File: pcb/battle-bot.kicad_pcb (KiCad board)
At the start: 4 copper layers, 0 parts

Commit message: Place power connectors
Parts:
- added REF**: AMASS_XT30PW-M_1x02_P2.50mm_Horizontal, Connector_AMASS:AMASS_XT30PW-M_1x02_P2.50mm_Horizontal, F.Cu at (73.2, 53.8)
- added REF**: AMASS_XT30PW-M_1x02_P2.50mm_Horizontal, Connector_AMASS:AMASS_XT30PW-M_1x02_P2.50mm_Horizontal, F.Cu at (132.7, 56.6)
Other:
- board outline added: 99.2 x 51.2 mm

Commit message: Save
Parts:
- added C1: 22u, Capacitor_SMD:C_1206_3216Metric, F.Cu at (154.3, 87.5)
- added C2: 22u, Capacitor_SMD:C_1206_3216Metric, F.Cu at (154.3, 90.8)
- added C3: 10n, Capacitor_SMD:C_0402_1005Metric, F.Cu at (165.1, 69.9)
- added C4: 47u, Capacitor_SMD:C_1206_3216Metric, F.Cu at (154.3, 94.2)
- added C5: 47u, Capacitor_SMD:C_1206_3216Metric, F.Cu at (154.3, 97.5)
- added C6: 47u, Capacitor_SMD:C_1206_3216Metric, F.Cu at (154.3, 100.9)
- added D3: B5819W, Diode_SMD:D_SOD-123, F.Cu at (160.1, 101.8)
- added L1: 15u, Inductor_SMD:L_Changjiang_FNR6020S, F.Cu at (161.0, 96.3)
- added R1: R, Resistor_SMD:R_0402_1005Metric, F.Cu at (164.4, 101.1)
- added R2: R, Resistor_SMD:R_0402_1005Metric, F.Cu at (164.4, 103.1)
- added REF**: BGA-16_1.92x1.92mm_Layout4x4_P0.5mm, Package_BGA:BGA-16_1.92x1.92mm_Layout4x4_P0.5mm, F.Cu at (92.0, 67.3)
- added REF**: BGA-16_1.92x1.92mm_Layout4x4_P0.5mm, Package_BGA:BGA-16_1.92x1.92mm_Layout4x4_P0.5mm, F.Cu at (108.0, 71.8)
- added REF**: BGA-16_1.92x1.92mm_Layout4x4_P0.5mm, Package_BGA:BGA-16_1.92x1.92mm_Layout4x4_P0.5mm, F.Cu at (86.8, 71.8)
- added REF**: BGA-16_1.92x1.92mm_Layout4x4_P0.5mm, Package_BGA:BGA-16_1.92x1.92mm_Layout4x4_P0.5mm, F.Cu at (102.7, 67.3)
- added REF**: BGA-16_1.92x1.92mm_Layout4x4_P0.5mm, Package_BGA:BGA-16_1.92x1.92mm_Layout4x4_P0.5mm, F.Cu at (113.3, 71.8)
- added REF**: TFBGA-100_8x8mm_Layout10x10_P0.8mm, Package_BGA:TFBGA-100_8x8mm_Layout10x10_P0.8mm, F.Cu at (160.4, 79.2)
- added REF**: PowerPAK_SO-8_Single, Package_SO:PowerPAK_SO-8_Single, F.Cu at (126.4, 61.9)
- added REF**: R_0402_1005Metric, Resistor_SMD:R_0402_1005Metric, F.Cu at (92.6, 64.5)
- added REF**: BGA-16_1.92x1.92mm_Layout4x4_P0.5mm, Package_BGA:BGA-16_1.92x1.92mm_Layout4x4_P0.5mm, F.Cu at (113.3, 67.2)
- added REF**: PowerPAK_SO-8_Single, Package_SO:PowerPAK_SO-8_Single, F.Cu at (74.4, 61.7)
- added REF**: BGA-16_1.92x1.92mm_Layout4x4_P0.5mm, Package_BGA:BGA-16_1.92x1.92mm_Layout4x4_P0.5mm, F.Cu at (97.3, 71.8)
- added REF**: BGA-16_1.92x1.92mm_Layout4x4_P0.5mm, Package_BGA:BGA-16_1.92x1.92mm_Layout4x4_P0.5mm, F.Cu at (92.0, 71.8)
- added REF**: BGA-16_1.92x1.92mm_Layout4x4_P0.5mm, Package_BGA:BGA-16_1.92x1.92mm_Layout4x4_P0.5mm, F.Cu at (102.7, 71.8)
- added U1: TPS5430DDA, Package_SO:TI_SO-PowerPAD-8_ThermalVias, F.Cu at (161.4, 89.2)
- added U2: STM32G474VETx, Package_QFP:LQFP-100_14x14mm_P0.5mm, F.Cu at (100.0, 49.4)
- moved REF** 5.72 mm to (127.6, 54.0)
- moved REF** 4.08 mm to (76.7, 51.7)

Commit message: Finish drivers
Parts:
- removed REF** (x9): BGA-16_1.92x1.92mm_Layout4x4_P0.5mm, Package_BGA:BGA-16_1.92x1.92mm_Layout4x4_P0.5mm
- removed REF** (x2): AMASS_XT30PW-M_1x02_P2.50mm_Horizontal, Connector_AMASS:AMASS_XT30PW-M_1x02_P2.50mm_Horizontal
- removed REF**: TFBGA-100_8x8mm_Layout10x10_P0.8mm, Package_BGA:TFBGA-100_8x8mm_Layout10x10_P0.8mm
- removed REF** (x2): PowerPAK_SO-8_Single, Package_SO:PowerPAK_SO-8_Single
- removed REF**: R_0402_1005Metric, Resistor_SMD:R_0402_1005Metric
- added AE1: Antenna, RF_Antenna:Johanson_2450AT18x100, F.Cu at (120.8, 7.26)
- added C10: 100n, Resistor_SMD:R_0402_1005Metric, F.Cu at (134.7, 13.1)
- added C11: 47u, Capacitor_SMD:C_1206_3216Metric, F.Cu at (117.6, 37.7)
- added C12: 10n, Capacitor_SMD:C_0402_1005Metric, F.Cu at (130.3, 5.78)
- added C13: 33n, Capacitor_SMD:C_0402_1005Metric, F.Cu at (131.7, 7.17)
- added C14: 47u, Capacitor_SMD:C_1206_3216Metric, F.Cu at (117.6, 41.0)
- added C15: 1n, Capacitor_SMD:C_0402_1005Metric, F.Cu at (125.9, 3.86)
- added C16: 47u, Capacitor_SMD:C_1206_3216Metric, F.Cu at (117.6, 44.3)
- added C17: 47u, Capacitor_SMD:C_1206_3216Metric, F.Cu at (117.6, 47.6)
- added C18: 220u, Capacitor_THT:C_Radial_D6.3mm_H7.0mm_P2.50mm, F.Cu at (97.7, 42.8)
- added C19: 2n2, Capacitor_SMD:C_0603_1608Metric, F.Cu at (128.0, 12.1)
- added C20: 12p, Capacitor_SMD:C_0402_1005Metric, F.Cu at (123.6, 12.6)
- added C21: 4p7, Capacitor_SMD:C_0603_1608Metric, F.Cu at (129.8, 13.9)
- added C22: 1p5, Capacitor_SMD:C_0402_1005Metric, F.Cu at (126.4, 15.4)
- added C23: 12p, Capacitor_SMD:C_0402_1005Metric, F.Cu at (122.2, 11.2)
- added C24: 1p, Capacitor_SMD:C_0402_1005Metric, F.Cu at (125.0, 14.0)
- added C25: 10u, Resistor_SMD:R_0402_1005Metric, F.Cu at (136.1, 14.5)
- added C26: 4u7, Capacitor_SMD:C_0402_1005Metric, F.Cu at (119.7, -1.48)
- added C27: 10n, Capacitor_SMD:C_0402_1005Metric, F.Cu at (127.9, 1.83)
- added C28: 220p, Resistor_SMD:R_0402_1005Metric, F.Cu at (137.5, 15.9)
- added C29: 100n, Capacitor_SMD:C_0402_1005Metric, F.Cu at (121.5, 0.22)
- added C30: 100n, Capacitor_SMD:C_0402_1005Metric, F.Cu at (122.9, 1.61)
- added C31: 0p3, Capacitor_SMD:C_0402_1005Metric, F.Cu at (135.8, 3.11)
- added C32: 22u, Resistor_SMD:R_0805_2012Metric, F.Cu at (66.1, 35.9)
- added C33: 1u, Resistor_SMD:R_0402_1005Metric, F.Cu at (65.4, 27.5)
- added C34: 1u, Resistor_SMD:R_0402_1005Metric, F.Cu at (65.4, 29.5)
- added C35: 100n, Capacitor_SMD:C_0402_1005Metric, F.Cu at (74.1, 27.5)
- added C36: 1u, Resistor_SMD:R_0402_1005Metric, F.Cu at (65.4, 31.5)
- added C37: 47n, Capacitor_SMD:C_0402_1005Metric, F.Cu at (74.1, 29.5)
- added C38: 100n, Capacitor_SMD:C_0402_1005Metric, F.Cu at (74.1, 31.4)
- added C39: 22u, Resistor_SMD:R_0805_2012Metric, F.Cu at (106.2, 27.9)
- added C40: 1u, Resistor_SMD:R_0402_1005Metric, F.Cu at (105.5, 19.5)
- added C41: 1u, Resistor_SMD:R_0402_1005Metric, F.Cu at (105.5, 21.5)
- added C42: 100n, Capacitor_SMD:C_0402_1005Metric, F.Cu at (114.2, 19.5)
- added C43: 1u, Resistor_SMD:R_0402_1005Metric, F.Cu at (105.5, 23.5)
- added C44: 47n, Capacitor_SMD:C_0402_1005Metric, F.Cu at (114.2, 21.5)
- added C45: 100n, Capacitor_SMD:C_0402_1005Metric, F.Cu at (114.2, 23.4)
- added C46: 22u, Resistor_SMD:R_0805_2012Metric, F.Cu at (80.0, 31.2)
- added C47: 1u, Resistor_SMD:R_0402_1005Metric, F.Cu at (79.2, 22.8)
- added C48: 1u, Resistor_SMD:R_0402_1005Metric, F.Cu at (79.2, 24.8)
- added C49: 100n, Capacitor_SMD:C_0402_1005Metric, F.Cu at (87.9, 22.8)
- added C50: 1u, Resistor_SMD:R_0402_1005Metric, F.Cu at (79.2, 26.8)
- added C51: 47n, Capacitor_SMD:C_0402_1005Metric, F.Cu at (87.9, 24.8)
- added C52: 100n, Capacitor_SMD:C_0402_1005Metric, F.Cu at (87.9, 26.7)
- added C53: 10u, Capacitor_SMD:C_0603_1608Metric, F.Cu at (105.8, 70.6)
- added C54: 100n, Capacitor_SMD:C_0402_1005Metric, F.Cu at (105.9, 69.4)
- added C55: 220n, Capacitor_SMD:C_0402_1005Metric, F.Cu at (105.2, 66.0)
- added C56: 10u, Capacitor_SMD:C_0603_1608Metric, F.Cu at (81.8, 70.6)
- added C57: 100n, Capacitor_SMD:C_0402_1005Metric, F.Cu at (81.9, 69.4)
- added C58: 220n, Capacitor_SMD:C_0402_1005Metric, F.Cu at (81.2, 66.0)
- added C59: 10u, Capacitor_SMD:C_0603_1608Metric, F.Cu at (93.8, 70.6)
- added C60: 100n, Capacitor_SMD:C_0402_1005Metric, F.Cu at (93.9, 69.4)
- added C61: 220n, Capacitor_SMD:C_0402_1005Metric, F.Cu at (93.2, 66.0)
- added C7: 100u, Resistor_SMD:R_1206_3216Metric, F.Cu at (137.4, 5.69)
- added C8: 10u, Resistor_SMD:R_0402_1005Metric, F.Cu at (133.3, 11.7)
- added C9: 100n, Capacitor_SMD:C_0402_1005Metric, F.Cu at (105.3, 34.8)
- added D1: LEDG, LED_SMD:LED_0603_1608Metric, F.Cu at (74.2, 33.8)
- added D2: LEDR, LED_SMD:LED_0603_1608Metric, F.Cu at (84.9, 54.2)
- added D4: LEDR, LED_SMD:LED_0603_1608Metric, F.Cu at (96.2, 55.7)
- added J1: Conn_01x02_Pin, Connector_AMASS:AMASS_XT30PW-M_1x02_P2.50mm_Horizontal, F.Cu at (74.5, 51.3)
- added J2: Conn_01x02_Pin, Connector_AMASS:AMASS_XT30PW-M_1x02_P2.50mm_Horizontal, F.Cu at (130.9, 55.4)
- added L2: 2n7, Inductor_SMD:L_0402_1005Metric, F.Cu at (121.6, 14.7)
- added L3: 8n2, Inductor_SMD:L_0402_1005Metric, F.Cu at (120.2, 13.3)
- added L4: 3n9, Inductor_SMD:L_0402_1005Metric, F.Cu at (123.0, 16.1)
- added Q10: AON7544, User_Footprints:DFN3x3A_8L_EP1_P, F.Cu at (127.0, 66.9)
- added Q11: AON7544, User_Footprints:DFN3x3A_8L_EP1_P, F.Cu at (127.1, 61.6)
- added Q12: AON7544, User_Footprints:DFN3x3A_8L_EP1_P, F.Cu at (129.7, 64.2)
- added Q13: AON7544, User_Footprints:DFN3x3A_8L_EP1_P, F.Cu at (121.7, 67.0)
- added Q14: AON7544, User_Footprints:DFN3x3A_8L_EP1_P, F.Cu at (124.3, 69.6)
- added Q15: AON7544, User_Footprints:DFN3x3A_8L_EP1_P, F.Cu at (86.6, 44.8)
- added Q16: AON7544, User_Footprints:DFN3x3A_8L_EP1_P, F.Cu at (84.0, 42.1)
- added Q17: AON7544, User_Footprints:DFN3x3A_8L_EP1_P, F.Cu at (83.9, 47.5)
- added Q18: AON7544, User_Footprints:DFN3x3A_8L_EP1_P, F.Cu at (81.3, 44.8)
- added Q19: AON7544, User_Footprints:DFN3x3A_8L_EP1_P, F.Cu at (89.3, 42.0)
- added Q20: AON7544, User_Footprints:DFN3x3A_8L_EP1_P, F.Cu at (86.7, 39.4)
- added Q21: GANE3R9, User_Footprints:GANE3R9, F.Cu at (111.8, 66.7)
- added Q22: GANE3R9, User_Footprints:GANE3R9, F.Cu at (110.7, 71.9)
- added Q23: GANE3R9, User_Footprints:GANE3R9, F.Cu at (87.8, 66.7)
- added Q24: GANE3R9, User_Footprints:GANE3R9, F.Cu at (86.7, 71.9)
- added Q25: GANE3R9, User_Footprints:GANE3R9, F.Cu at (99.8, 66.7)
- added Q26: GANE3R9, User_Footprints:GANE3R9, F.Cu at (98.7, 71.9)
- added Q3: AON7544, User_Footprints:DFN3x3A_8L_EP1_P, F.Cu at (74.4, 63.4)
- added Q4: AON7544, User_Footprints:DFN3x3A_8L_EP1_P, F.Cu at (71.8, 66.0)
- added Q5: AON7544, User_Footprints:DFN3x3A_8L_EP1_P, F.Cu at (77.1, 66.1)
- added Q6: AON7544, User_Footprints:DFN3x3A_8L_EP1_P, F.Cu at (74.5, 68.7)
- added Q7: AON7544, User_Footprints:DFN3x3A_8L_EP1_P, F.Cu at (71.7, 60.7)
- added Q8: AON7544, User_Footprints:DFN3x3A_8L_EP1_P, F.Cu at (69.0, 63.3)
- added Q9: AON7544, User_Footprints:DFN3x3A_8L_EP1_P, F.Cu at (124.4, 64.3)
- added R10: 1k, Resistor_SMD:R_0402_1005Metric, F.Cu at (127.2, 20.3)
- added R11: 1k, Resistor_SMD:R_0402_1005Metric, F.Cu at (124.4, 17.5)
- added R12: 22k, Resistor_SMD:R_0402_1005Metric, F.Cu at (125.8, 18.9)
- added R13: 47k, Resistor_SMD:R_0402_1005Metric, F.Cu at (65.4, 33.5)
- added R14: 1k, Resistor_SMD:R_0402_1005Metric, F.Cu at (68.3, 27.5)
- added R15: 510k, Resistor_SMD:R_0402_1005Metric, F.Cu at (84.3, 56.5)
- added R16: 47k, Resistor_SMD:R_0402_1005Metric, F.Cu at (68.3, 29.5)
- added R17: 510k, Resistor_SMD:R_0402_1005Metric, F.Cu at (84.3, 58.5)
- added R18: R, Resistor_SMD:R_0402_1005Metric, F.Cu at (67.0, 66.8)
- added R19: 2m, Resistor_SMD:R_1206_3216Metric, F.Cu at (70.5, 70.2)
- added R20: 47k, Resistor_SMD:R_0402_1005Metric, F.Cu at (105.5, 25.5)
- added R21: 1k, Resistor_SMD:R_0402_1005Metric, F.Cu at (108.4, 19.5)
- added R22: 510k, Resistor_SMD:R_0402_1005Metric, F.Cu at (120.6, 53.9)
- added R23: 47k, Resistor_SMD:R_0402_1005Metric, F.Cu at (108.4, 21.5)
- added R24: 510k, Resistor_SMD:R_0402_1005Metric, F.Cu at (122.6, 53.9)
- added R25: R, Resistor_SMD:R_0402_1005Metric, F.Cu at (128.6, 71.6)
- added R26: 2m, Resistor_SMD:R_1206_3216Metric, F.Cu at (132.5, 67.8)
- added R27: 47k, Resistor_SMD:R_0402_1005Metric, F.Cu at (79.2, 28.8)
- added R28: 1k, Resistor_SMD:R_0402_1005Metric, F.Cu at (82.1, 22.8)
- added R29: 510k, Resistor_SMD:R_0402_1005Metric, F.Cu at (93.9, 55.1)
- added R3: 100k, Resistor_SMD:R_0402_1005Metric, F.Cu at (102.9, 37.3)
- added R30: 47k, Resistor_SMD:R_0402_1005Metric, F.Cu at (82.1, 24.8)
- added R31: 510k, Resistor_SMD:R_0402_1005Metric, F.Cu at (92.0, 55.1)
- added R32: 10R, Resistor_SMD:R_0402_1005Metric, F.Cu at (82.6, 37.3)
- added R33: 2m, Resistor_SMD:R_1206_3216Metric, F.Cu at (78.6, 41.0)
- added R34: 10R, Resistor_SMD:R_0402_1005Metric, F.Cu at (107.1, 66.0)
- added R35: 10R, Resistor_SMD:R_0402_1005Metric, F.Cu at (107.9, 68.3)
- added R36: 10R, Resistor_SMD:R_0402_1005Metric, F.Cu at (83.1, 66.0)
- added R37: 10R, Resistor_SMD:R_0402_1005Metric, F.Cu at (83.9, 68.3)
- added R38: 10R, Resistor_SMD:R_0402_1005Metric, F.Cu at (95.1, 66.0)
- added R4: 100k, Resistor_SMD:R_0402_1005Metric, F.Cu at (107.6, 32.8)
- added R43: 10R, Resistor_SMD:R_0402_1005Metric, F.Cu at (68.3, 31.5)
- added R44: 10R, Resistor_SMD:R_0402_1005Metric, F.Cu at (108.4, 23.5)
- added R45: 10R, Resistor_SMD:R_0402_1005Metric, F.Cu at (82.1, 26.8)
- added R46: 10R, Resistor_SMD:R_0402_1005Metric, F.Cu at (68.3, 33.5)
- added R47: 10R, Resistor_SMD:R_0402_1005Metric, F.Cu at (108.4, 25.5)
- added R48: 10R, Resistor_SMD:R_0402_1005Metric, F.Cu at (82.1, 28.8)
- added R49: 10R, Resistor_SMD:R_0402_1005Metric, F.Cu at (71.2, 27.5)
- added R5: 15k, Resistor_SMD:R_0402_1005Metric, F.Cu at (107.6, 34.8)
- added R50: 10R, Resistor_SMD:R_0402_1005Metric, F.Cu at (111.3, 19.5)
- added R51: 10R, Resistor_SMD:R_0402_1005Metric, F.Cu at (85.0, 22.8)
- added R52: 10R, Resistor_SMD:R_0402_1005Metric, F.Cu at (71.2, 29.5)
- added R53: 10R, Resistor_SMD:R_0402_1005Metric, F.Cu at (111.3, 21.5)
- added R54: 10R, Resistor_SMD:R_0402_1005Metric, F.Cu at (85.0, 24.8)
- added R55: 10R, Resistor_SMD:R_0402_1005Metric, F.Cu at (71.2, 31.5)
- added R56: 10R, Resistor_SMD:R_0402_1005Metric, F.Cu at (111.3, 23.5)
- added R57: 10R, Resistor_SMD:R_0402_1005Metric, F.Cu at (85.0, 26.8)
- added R58: 10R, Resistor_SMD:R_0402_1005Metric, F.Cu at (71.2, 33.5)
- added R59: 10R, Resistor_SMD:R_0402_1005Metric, F.Cu at (111.3, 25.5)
- added R6: 22k, Resistor_SMD:R_0402_1005Metric, F.Cu at (136.7, 0.04)
- added R60: 10R, Resistor_SMD:R_0402_1005Metric, F.Cu at (85.0, 28.8)
- added R7: 10k, Resistor_SMD:R_0402_1005Metric, F.Cu at (110.0, 32.8)
- added R8: 100k, Resistor_SMD:R_0402_1005Metric, F.Cu at (110.0, 34.8)
- added R9: 1k, Resistor_SMD:R_0402_1005Metric, F.Cu at (73.7, 36.1)
- added U10: LMG1205, User_Footprints:LMG1205, F.Cu at (106.2, 67.7)
- added U11: LMG1205, User_Footprints:LMG1205, F.Cu at (82.2, 67.7)
- added U12: LMG1205, User_Footprints:LMG1205, F.Cu at (94.2, 67.7)
- added U13: ACS780xLRTR-100B, Sensor_Current:Allegro_PSOF-7_4.8x6.4mm_P1.60mm, F.Cu at (95.7, 25.9)
- added U3: AT2401C, Package_DFN_QFN:QFN-16-1EP_3x3mm_P0.5mm_EP1.7x1.7mm, F.Cu at (132.0, 0.12)
- added U4: ICM-42688-P, Package_LGA:LGA-14_3x2.5mm_P0.5mm_LayoutBorder3x4y, F.Cu at (124.6, -1.38)
- added U5: LFL152G45TC1A219, User_Footprints:LFL152G45TC1A219, F.Cu at (135.8, -1.03)
- added U6: STM32G431RBTx, Package_QFP:LQFP-64_10x10mm_P0.5mm, F.Cu at (146.5, 11.8)
- added U7: DRV8323H, Package_DFN_QFN:HVQFN-40-1EP_6x6mm_P0.5mm_EP4.1x4.1mm, F.Cu at (79.7, 57.5)
- added U8: DRV8323H, Package_DFN_QFN:HVQFN-40-1EP_6x6mm_P0.5mm_EP4.1x4.1mm, F.Cu at (118.5, 59.0)
- added U9: DRV8323H, Package_DFN_QFN:HVQFN-40-1EP_6x6mm_P0.5mm_EP4.1x4.1mm, F.Cu at (92.5, 50.1)
- added Y1: 16MHz, Crystal:Crystal_SMD_3225-4Pin_3.2x2.5mm, F.Cu at (126.0, 9.21)
- C1, C2: footprint Capacitor_SMD:C_1206_3216Metric -> Capacitor_SMD:C_0805_2012Metric
- C3: value 10n -> 22u; footprint Capacitor_SMD:C_0402_1005Metric -> Capacitor_SMD:C_0805_2012Metric
- C4: value 47u -> 22u; footprint Capacitor_SMD:C_1206_3216Metric -> Capacitor_SMD:C_0805_2012Metric
- C5, C6: value 47u -> 1u; footprint Capacitor_SMD:C_1206_3216Metric -> Capacitor_SMD:C_0402_1005Metric
- D3: value B5819W -> LEDR; footprint Diode_SMD:D_SOD-123 -> LED_SMD:LED_0603_1608Metric
- L1: value 15u -> 1u; footprint Inductor_SMD:L_Changjiang_FNR6020S -> Inductor_SMD:L_Changjiang_FXL0630
- R1: value R -> 22k
- R2: value R -> 10k
- U1: value TPS5430DDA -> TPS53319; footprint Package_SO:TI_SO-PowerPAD-8_ThermalVias -> Package_DFN_QFN:DFN-22-1EP_5x6mm_P0.5mm_EP3.14x4.3mm
- U2: value STM32G474VETx -> nRF24L01P; footprint Package_QFP:LQFP-100_14x14mm_P0.5mm -> Package_DFN_QFN:QFN-20-1EP_4x4mm_P0.5mm_EP2.5x2.5mm
- moved R2 88.1 mm to (102.9, 40.0)
- moved R1 85.3 mm to (102.9, 42.0)
- moved C6 83.4 mm to (100.3, 37.4)
- moved C5 82.3 mm to (100.3, 35.4)
- moved L1 73.4 mm to (106.0, 47.7)
- moved U1 73.3 mm to (107.6, 39.5)
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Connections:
- C1 pad 1: Net-(D1-K) -> VDD
- C2 pad 1: Net-(D1-K) -> VDD
- C3 pad 1: /BT -> VDD
- C3 pad 2: Net-(D3-K) -> GND
- C4 pad 1: +5V -> VDD
- C5 pad 1: +5V -> VDD
- C6 pad 1: +5V -> Net-(U1-VREG)
- D3 pad 2: GND -> +5V
- L1 pad 1: Net-(D3-K) -> Net-(C9-Pad1)
- R1 pad 1: +5V -> /REN
- R1 pad 2: /VSNS -> VDD
- R2 pad 1: /VSNS -> GND
- R2 pad 2: GND -> /REN
- U1 pad 1: /BT -> Net-(U1-VFB)
- U1 pad 2: unconnected-(U1-NC-Pad2) -> /REN
- U1 pad 3: unconnected-(U1-NC-Pad3) -> /PGD
- U1 pad 4: /VSNS -> Net-(U1-VBST)
- U1 pad 5: unconnected-(U1-EN-Pad5) -> GND
- U1 pad 6: GND -> Net-(C9-Pad1)
- U1 pad 7: Net-(D1-K) -> Net-(C9-Pad1)
- U1 pad 8: Net-(D3-K) -> Net-(C9-Pad1)
- U1 pad 9: GND -> Net-(C9-Pad1)
- U2 pad 1: unconnected-(U2-PE2-Pad1) -> /RCE
- U2 pad 10: unconnected-(U2-PF9-Pad10) -> /XC1
- U2 pad 11: unconnected-(U2-PF10-Pad11) -> /VPA
- U2 pad 12: unconnected-(U2-PF0-Pad12) -> Net-(U2-ANT1)
- U2 pad 13: unconnected-(U2-PF1-Pad13) -> Net-(U2-ANT2)
- U2 pad 14: unconnected-(U2-PG10-Pad14) -> GND
- U2 pad 15: unconnected-(U2-PC0-Pad15) -> +3V3
- U2 pad 16: unconnected-(U2-PC1-Pad16) -> Net-(U2-IREF)
- U2 pad 17: unconnected-(U2-PC2-Pad17) -> GND
- U2 pad 18: unconnected-(U2-PC3-Pad18) -> +3V3
- U2 pad 19: unconnected-(U2-PF2-Pad19) -> Net-(U2-DVDD)
- U2 pad 2: unconnected-(U2-PE3-Pad2) -> /RCS
- U2 pad 20: unconnected-(U2-PA0-Pad20) -> GND
- U2 pad 21: unconnected-(U2-PA1-Pad21) -> GND
- U2 pad 3: unconnected-(U2-PE4-Pad3) -> /CLK
- U2 pad 4: unconnected-(U2-PE5-Pad4) -> /MOSI
- U2 pad 5: unconnected-(U2-PE6-Pad5) -> /MISO
- U2 pad 6: unconnected-(U2-VBAT-Pad6) -> /RIRQ
- U2 pad 7: unconnected-(U2-PC13-Pad7) -> +3V3
- U2 pad 8: unconnected-(U2-PC14-Pad8) -> GND
- U2 pad 9: unconnected-(U2-PC15-Pad9) -> /XC2
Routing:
- net +5V: track 0.00 -> 8.11 mm
- net GND: track 0.00 -> 7.17 mm
- net /LargeMotor/LargeBridgeC/OUT: track 0.00 -> 3.77 mm
- net /LargeMotor/LargeBridgeB/OUT: track 0.00 -> 3.77 mm
- net /LargeMotor/LargeBridgeA/OUT: track 0.00 -> 3.77 mm
- net Net-(U12-HOL): track 0.00 -> 3.13 mm
- net Net-(U11-HOL): track 0.00 -> 3.13 mm
- net Net-(U10-HOL): track 0.00 -> 3.13 mm
- net Net-(U11-LOL): track 0.00 -> 2.94 mm
- net Net-(U12-LOL): track 0.00 -> 2.94 mm
- net Net-(U10-LOL): track 0.00 -> 2.94 mm
- net Net-(U11-HOH): track 0.00 -> 1.25 mm
- net Net-(U12-HOH): track 0.00 -> 1.25 mm
- net Net-(U10-HOH): track 0.00 -> 1.25 mm
- net Net-(U12-HB): track 0.00 -> 1.23 mm
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
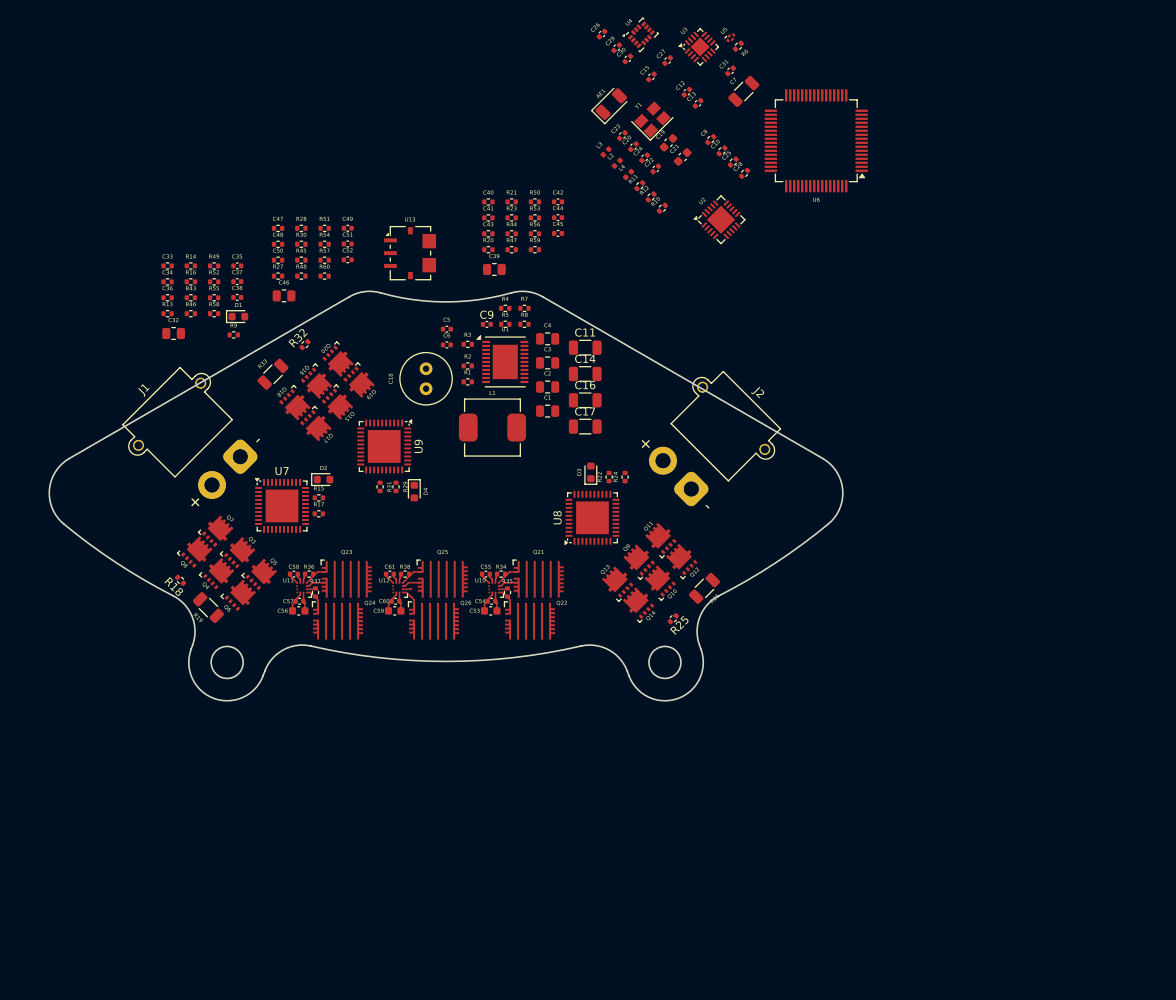
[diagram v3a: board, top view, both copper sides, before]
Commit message: Finish rough layout
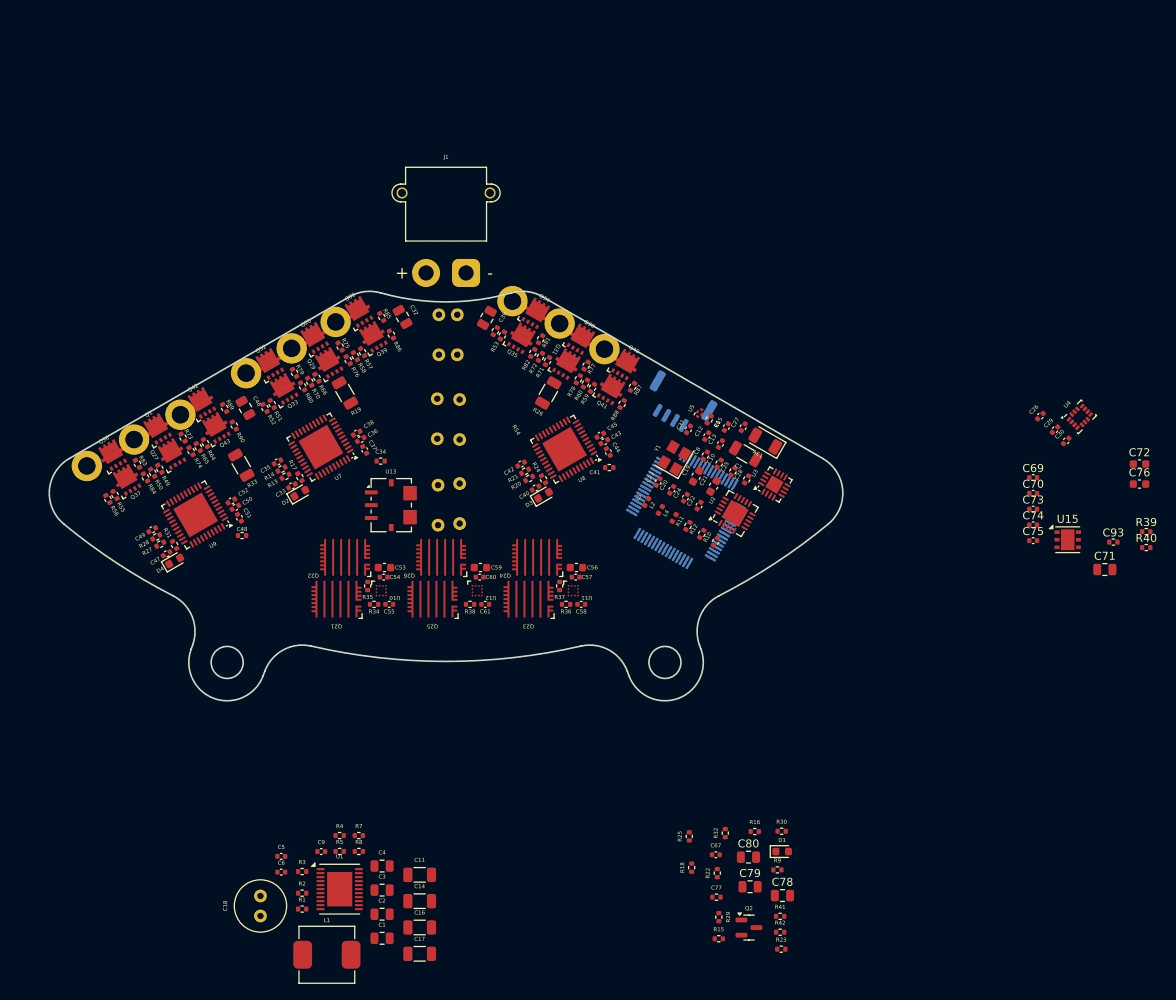
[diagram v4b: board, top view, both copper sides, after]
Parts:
- removed Q10, Q11, Q12, Q13, Q14, Q15, Q16, Q17, Q18, Q19, Q20, Q3, Q4, Q5, Q6, Q7, Q8, Q9: AON7544, User_Footprints:DFN3x3A_8L_EP1_P
- removed R43, R44, R45, R46, R47, R48: 10R, Resistor_SMD:R_0402_1005Metric
- added ?: , , F.Cu at (108.5, 31.9)
- added ?: , , F.Cu at (120.0, 37.9)
- added ?: , , F.Cu at (114.4, 34.7)
- added C67: C, Capacitor_SMD:C_0402_1005Metric, F.Cu at (133.9, 101.1)
- added C68: 2m2, Capacitor_THT:C_Radial_D10.0mm_H16.0mm_P5.00mm, B.Cu at (99.2, 54.9)
- added C68: 2m2, Capacitor_THT:C_Radial_D10.0mm_H16.0mm_P5.00mm, B.Cu at (99.1, 44.1)
- added C68: 2m2, Capacitor_THT:C_Radial_D10.0mm_H16.0mm_P5.00mm, B.Cu at (101.9, 49.2)
- added C68: 2m2, Capacitor_THT:C_Radial_D10.0mm_H16.0mm_P5.00mm, B.Cu at (101.9, 59.7)
- added C68: 2m2, Capacitor_THT:C_Radial_D10.0mm_H16.0mm_P5.00mm, B.Cu at (101.6, 38.6)
- added C68: 2m2, Capacitor_THT:C_Radial_D10.0mm_H16.0mm_P5.00mm, B.Cu at (99.3, 33.6)
- added C69: 100n, Capacitor_SMD:C_0402_1005Metric, F.Cu at (173.6, 54.0)
- added C70: 100n, Capacitor_SMD:C_0402_1005Metric, F.Cu at (173.6, 55.9)
- added C71: 22u, Capacitor_SMD:C_0805_2012Metric, F.Cu at (182.6, 65.4)
- added C72: 22u, Capacitor_SMD:C_0603_1608Metric, F.Cu at (186.9, 52.3)
- added C73: 2u2, Capacitor_SMD:C_0402_1005Metric, F.Cu at (173.6, 57.9)
- added C74: 100n, Capacitor_SMD:C_0402_1005Metric, F.Cu at (173.6, 59.9)
- added C75: 100n, Capacitor_SMD:C_0402_1005Metric, F.Cu at (173.6, 61.8)
- added C76: 10u, Capacitor_SMD:C_0603_1608Metric, F.Cu at (186.9, 54.8)
- added C77: 220p, Resistor_SMD:R_0402_1005Metric, F.Cu at (134.0, 106.4)
- added C78: 22u, Capacitor_SMD:C_0805_2012Metric, F.Cu at (142.2, 106.2)
- added C79: 22u, Capacitor_SMD:C_0805_2012Metric, F.Cu at (138.2, 105.1)
- added C80: 22u, Capacitor_SMD:C_0805_2012Metric, F.Cu at (138.0, 101.4)
- added C93: 10u, Resistor_SMD:R_0402_1005Metric, F.Cu at (183.6, 62.0)
- added Q1: AON7544, User_Footprints:DFN3x3A_8L_EP1_P, F.Cu at (64.1, 47.9)
- added Q2: AO3401A, Package_TO_SOT_SMD:SOT-23, F.Cu at (138.1, 110.2)
- added Q27: AON7544, User_Footprints:DFN3x3A_8L_EP1_P, F.Cu at (65.9, 51.0)
- added Q28: AON7544, User_Footprints:DFN3x3A_8L_EP1_P, F.Cu at (83.8, 36.5)
- added Q29: AON7544, User_Footprints:DFN3x3A_8L_EP1_P, F.Cu at (85.6, 39.6)
- added Q30: AON7544, User_Footprints:DFN3x3A_8L_EP1_P, F.Cu at (117.0, 36.7)
- added Q31: AON7544, User_Footprints:DFN3x3A_8L_EP1_P, F.Cu at (115.2, 39.8)
- added Q32: AON7544, User_Footprints:DFN3x3A_8L_EP1_P, F.Cu at (78.2, 39.8)
- added Q33: AON7544, User_Footprints:DFN3x3A_8L_EP1_P, F.Cu at (80.0, 42.9)
- added Q34: AON7544, User_Footprints:DFN3x3A_8L_EP1_P, F.Cu at (111.4, 33.4)
- added Q35: AON7544, User_Footprints:DFN3x3A_8L_EP1_P, F.Cu at (109.6, 36.5)
- added Q36: AON7544, User_Footprints:DFN3x3A_8L_EP1_P, F.Cu at (58.5, 51.1)
- added Q37: AON7544, User_Footprints:DFN3x3A_8L_EP1_P, F.Cu at (60.3, 54.3)
- added Q38: AON7544, User_Footprints:DFN3x3A_8L_EP1_P, F.Cu at (89.3, 33.3)
- added Q39: AON7544, User_Footprints:DFN3x3A_8L_EP1_P, F.Cu at (91.1, 36.4)
- added Q40: AON7544, User_Footprints:DFN3x3A_8L_EP1_P, F.Cu at (122.6, 39.8)
- added Q41: AON7544, User_Footprints:DFN3x3A_8L_EP1_P, F.Cu at (120.8, 43.0)
- added Q42: AON7544, User_Footprints:DFN3x3A_8L_EP1_P, F.Cu at (69.7, 44.6)
- added Q43: AON7544, User_Footprints:DFN3x3A_8L_EP1_P, F.Cu at (71.5, 47.7)
- added R39: 2k2, Resistor_SMD:R_0402_1005Metric, F.Cu at (187.7, 60.7)
- added R40: 2k2, Resistor_SMD:R_0402_1005Metric, F.Cu at (187.7, 62.7)
- added R41: 1k, Resistor_SMD:R_0402_1005Metric, F.Cu at (142.0, 108.8)
- added R42: R, Resistor_SMD:R_0402_1005Metric, F.Cu at (142.0, 110.8)
- added R64: 4k7, Resistor_SMD:R_0402_1005Metric, F.Cu at (70.1, 49.7)
- added R65: 1k, Resistor_SMD:R_0402_1005Metric, F.Cu at (69.2, 50.2)
- added R66: 4k7, Resistor_SMD:R_0402_1005Metric, F.Cu at (84.1, 41.5)
- added R70: 1k, Resistor_SMD:R_0402_1005Metric, F.Cu at (83.2, 42.0)
- added R71: 4k7, Resistor_SMD:R_0402_1005Metric, F.Cu at (112.9, 39.4)
- added R72: 1k, Resistor_SMD:R_0402_1005Metric, F.Cu at (112.0, 38.9)
- added R73: 10R, Resistor_SMD:R_0402_1005Metric, F.Cu at (67.3, 49.0)
- added R74: 10R, Resistor_SMD:R_0402_1005Metric, F.Cu at (68.3, 50.7)
- added R75: 10R, Resistor_SMD:R_0402_1005Metric, F.Cu at (87.0, 37.6)
- added R76: 10R, Resistor_SMD:R_0402_1005Metric, F.Cu at (88.0, 39.3)
- added R77: 10R, Resistor_SMD:R_0402_1005Metric, F.Cu at (117.7, 40.0)
- added R78: 10R, Resistor_SMD:R_0402_1005Metric, F.Cu at (116.7, 41.7)
- added R79: 10R, Resistor_SMD:R_0402_1005Metric, F.Cu at (81.3, 40.9)
- added R80: 10R, Resistor_SMD:R_0402_1005Metric, F.Cu at (82.3, 42.6)
- added R81: 10R, Resistor_SMD:R_0402_1005Metric, F.Cu at (112.0, 36.7)
- added R82: 10R, Resistor_SMD:R_0402_1005Metric, F.Cu at (111.0, 38.4)
- added R83: 10R, Resistor_SMD:R_0402_1005Metric, F.Cu at (61.6, 52.2)
- added R84: 10R, Resistor_SMD:R_0402_1005Metric, F.Cu at (62.6, 53.9)
- added R85: 10R, Resistor_SMD:R_0402_1005Metric, F.Cu at (92.2, 33.9)
- added R86: 10R, Resistor_SMD:R_0402_1005Metric, F.Cu at (93.4, 36.1)
- added R87: 10R, Resistor_SMD:R_0402_1005Metric, F.Cu at (123.5, 42.6)
- added R88: 10R, Resistor_SMD:R_0402_1005Metric, F.Cu at (122.2, 44.7)
- added R89: 10R, Resistor_SMD:R_0402_1005Metric, F.Cu at (72.5, 45.3)
- added R90: 10R, Resistor_SMD:R_0402_1005Metric, F.Cu at (73.7, 47.5)
- added REF**: MountingHole_2.2mm_M2_DIN965_Pad, MountingHole:MountingHole_2.2mm_M2_DIN965_Pad, F.Cu at (55.3, 52.5)
- added REF**: MountingHole_2.2mm_M2_DIN965_Pad, MountingHole:MountingHole_2.2mm_M2_DIN965_Pad, F.Cu at (67.0, 46.1)
- added REF**: MountingHole_2.2mm_M2_DIN965_Pad, MountingHole:MountingHole_2.2mm_M2_DIN965_Pad, F.Cu at (86.4, 34.5)
- added REF**: MountingHole_2.2mm_M2_DIN965_Pad, MountingHole:MountingHole_2.2mm_M2_DIN965_Pad, F.Cu at (75.2, 40.9)
- added REF**: MountingHole_2.2mm_M2_DIN965_Pad, MountingHole:MountingHole_2.2mm_M2_DIN965_Pad, F.Cu at (61.2, 49.2)
- added REF**: MountingHole_2.2mm_M2_DIN965_Pad, MountingHole:MountingHole_2.2mm_M2_DIN965_Pad, F.Cu at (80.9, 37.8)
- added U15: LP38690SD, Package_DFN_QFN:DFN-6-1EP_3x3mm_P0.95mm_EP1.7x2.6mm, F.Cu at (177.9, 61.7)
- C32, C39, C46: footprint Resistor_SMD:R_0805_2012Metric -> Capacitor_SMD:C_0805_2012Metric
- C33, C36, C40, C43, C47, C50: footprint Resistor_SMD:R_0402_1005Metric -> Capacitor_SMD:C_0402_1005Metric
- J2: value Conn_01x02_Pin -> Conn_01x04_MountingPin; footprint Connector_AMASS:AMASS_XT30PW-M_1x02_P2.50mm_Horizontal -> Connector_JST:JST_GH_SM04B-GHS-TB_1x04-1MP_P1.25mm_Horizontal; moved to B.Cu
- R15, R22, R29: value 510k -> 4k7
- R16, R23, R30: value 47k -> 1k
- R17, R24, R31: value 510k -> 15k
- R18: value R -> 10k
- R25: value R -> 47k
- R49, R51, R53, R55, R57, R59: value 10R -> 4k7
- R50, R52, R54, R56, R58, R60: value 10R -> 1k
- U6: moved to B.Cu
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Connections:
- C33 pad 1: Net-(U7-DVDD) -> /SmallMotor1/DVDD
- C40 pad 1: Net-(U8-DVDD) -> /SmallMotor2/DVDD
- C47 pad 1: Net-(U9-DVDD) -> /SmallMotor3/DVDD
- C55 pad 2: /LargeMotor/LargeBridgeA/OUT -> /LargeMotor/OUTA
- C58 pad 2: /LargeMotor/LargeBridgeB/OUT -> /LargeMotor/OUTB
- C61 pad 2: /LargeMotor/LargeBridgeC/OUT -> /LargeMotor/OUTC
- J2 pad 1: VDD -> +3V3
- J2 pad 2: GND -> /ESDA
- Q21 pad 11: /LargeMotor/LargeBridgeA/OUT -> /LargeMotor/OUTA
- Q21 pad 21: /LargeMotor/LargeBridgeA/OUT -> /LargeMotor/OUTA
- Q21 pad 23: /LargeMotor/LargeBridgeA/OUT -> /LargeMotor/OUTA
- Q21 pad 3: /LargeMotor/LargeBridgeA/OUT -> /LargeMotor/OUTA
- Q21 pad 4: /LargeMotor/LargeBridgeA/OUT -> /LargeMotor/OUTA
- Q21 pad 5: /LargeMotor/LargeBridgeA/OUT -> /LargeMotor/OUTA
- Q21 pad 6: /LargeMotor/LargeBridgeA/OUT -> /LargeMotor/OUTA
- Q21 pad 7: /LargeMotor/LargeBridgeA/OUT -> /LargeMotor/OUTA
- Q21 pad 9: /LargeMotor/LargeBridgeA/OUT -> /LargeMotor/OUTA
- Q22 pad 10: /LargeMotor/LargeBridgeA/OUT -> /LargeMotor/OUTA
- Q22 pad 12: /LargeMotor/LargeBridgeA/OUT -> /LargeMotor/OUTA
- Q22 pad 13: /LargeMotor/LargeBridgeA/OUT -> /LargeMotor/OUTA
- Q22 pad 14: /LargeMotor/LargeBridgeA/OUT -> /LargeMotor/OUTA
- Q22 pad 15: /LargeMotor/LargeBridgeA/OUT -> /LargeMotor/OUTA
- Q22 pad 16: /LargeMotor/LargeBridgeA/OUT -> /LargeMotor/OUTA
- Q22 pad 17: /LargeMotor/LargeBridgeA/OUT -> /LargeMotor/OUTA
- Q22 pad 18: /LargeMotor/LargeBridgeA/OUT -> /LargeMotor/OUTA
- Q22 pad 19: /LargeMotor/LargeBridgeA/OUT -> /LargeMotor/OUTA
- Q22 pad 20: /LargeMotor/LargeBridgeA/OUT -> /LargeMotor/OUTA
- Q22 pad 22: /LargeMotor/LargeBridgeA/OUT -> /LargeMotor/OUTA
- Q22 pad 24: /LargeMotor/LargeBridgeA/OUT -> /LargeMotor/OUTA
- Q22 pad 8: /LargeMotor/LargeBridgeA/OUT -> /LargeMotor/OUTA
- Q23 pad 11: /LargeMotor/LargeBridgeB/OUT -> /LargeMotor/OUTB
- Q23 pad 21: /LargeMotor/LargeBridgeB/OUT -> /LargeMotor/OUTB
- Q23 pad 23: /LargeMotor/LargeBridgeB/OUT -> /LargeMotor/OUTB
- Q23 pad 3: /LargeMotor/LargeBridgeB/OUT -> /LargeMotor/OUTB
- Q23 pad 4: /LargeMotor/LargeBridgeB/OUT -> /LargeMotor/OUTB
- Q23 pad 5: /LargeMotor/LargeBridgeB/OUT -> /LargeMotor/OUTB
- Q23 pad 6: /LargeMotor/LargeBridgeB/OUT -> /LargeMotor/OUTB
- Q23 pad 7: /LargeMotor/LargeBridgeB/OUT -> /LargeMotor/OUTB
- Q23 pad 9: /LargeMotor/LargeBridgeB/OUT -> /LargeMotor/OUTB
- Q24 pad 10: /LargeMotor/LargeBridgeB/OUT -> /LargeMotor/OUTB
- Q24 pad 11: /LargeMotor/LargeBridgeB/PL -> /LargeMotor/LargeBridgeA/PL
- Q24 pad 12: /LargeMotor/LargeBridgeB/OUT -> /LargeMotor/OUTB
- Q24 pad 13: /LargeMotor/LargeBridgeB/OUT -> /LargeMotor/OUTB
- Q24 pad 14: /LargeMotor/LargeBridgeB/OUT -> /LargeMotor/OUTB
- Q24 pad 15: /LargeMotor/LargeBridgeB/OUT -> /LargeMotor/OUTB
- Q24 pad 16: /LargeMotor/LargeBridgeB/OUT -> /LargeMotor/OUTB
- Q24 pad 17: /LargeMotor/LargeBridgeB/OUT -> /LargeMotor/OUTB
- Q24 pad 18: /LargeMotor/LargeBridgeB/OUT -> /LargeMotor/OUTB
- Q24 pad 19: /LargeMotor/LargeBridgeB/OUT -> /LargeMotor/OUTB
- Q24 pad 20: /LargeMotor/LargeBridgeB/OUT -> /LargeMotor/OUTB
- Q24 pad 21: /LargeMotor/LargeBridgeB/PL -> /LargeMotor/LargeBridgeA/PL
- Q24 pad 22: /LargeMotor/LargeBridgeB/OUT -> /LargeMotor/OUTB
- Q24 pad 23: /LargeMotor/LargeBridgeB/PL -> /LargeMotor/LargeBridgeA/PL
- Q24 pad 24: /LargeMotor/LargeBridgeB/OUT -> /LargeMotor/OUTB
- Q24 pad 3: /LargeMotor/LargeBridgeB/PL -> /LargeMotor/LargeBridgeA/PL
- Q24 pad 4: /LargeMotor/LargeBridgeB/PL -> /LargeMotor/LargeBridgeA/PL
- Q24 pad 5: /LargeMotor/LargeBridgeB/PL -> /LargeMotor/LargeBridgeA/PL
- Q24 pad 6: /LargeMotor/LargeBridgeB/PL -> /LargeMotor/LargeBridgeA/PL
- Q24 pad 7: /LargeMotor/LargeBridgeB/PL -> /LargeMotor/LargeBridgeA/PL
- Q24 pad 8: /LargeMotor/LargeBridgeB/OUT -> /LargeMotor/OUTB
- Q24 pad 9: /LargeMotor/LargeBridgeB/PL -> /LargeMotor/LargeBridgeA/PL
- Q25 pad 11: /LargeMotor/LargeBridgeC/OUT -> /LargeMotor/OUTC
- Q25 pad 21: /LargeMotor/LargeBridgeC/OUT -> /LargeMotor/OUTC
- Q25 pad 23: /LargeMotor/LargeBridgeC/OUT -> /LargeMotor/OUTC
- Q25 pad 3: /LargeMotor/LargeBridgeC/OUT -> /LargeMotor/OUTC
- Q25 pad 4: /LargeMotor/LargeBridgeC/OUT -> /LargeMotor/OUTC
- Q25 pad 5: /LargeMotor/LargeBridgeC/OUT -> /LargeMotor/OUTC
- Q25 pad 6: /LargeMotor/LargeBridgeC/OUT -> /LargeMotor/OUTC
- Q25 pad 7: /LargeMotor/LargeBridgeC/OUT -> /LargeMotor/OUTC
- Q25 pad 9: /LargeMotor/LargeBridgeC/OUT -> /LargeMotor/OUTC
- Q26 pad 10: /LargeMotor/LargeBridgeC/OUT -> /LargeMotor/OUTC
- Q26 pad 11: /LargeMotor/LargeBridgeC/PL -> /LargeMotor/LargeBridgeA/PL
- Q26 pad 12: /LargeMotor/LargeBridgeC/OUT -> /LargeMotor/OUTC
- Q26 pad 13: /LargeMotor/LargeBridgeC/OUT -> /LargeMotor/OUTC
- Q26 pad 14: /LargeMotor/LargeBridgeC/OUT -> /LargeMotor/OUTC
- Q26 pad 15: /LargeMotor/LargeBridgeC/OUT -> /LargeMotor/OUTC
- Q26 pad 16: /LargeMotor/LargeBridgeC/OUT -> /LargeMotor/OUTC
- Q26 pad 17: /LargeMotor/LargeBridgeC/OUT -> /LargeMotor/OUTC
- Q26 pad 18: /LargeMotor/LargeBridgeC/OUT -> /LargeMotor/OUTC
- Q26 pad 19: /LargeMotor/LargeBridgeC/OUT -> /LargeMotor/OUTC
- Q26 pad 20: /LargeMotor/LargeBridgeC/OUT -> /LargeMotor/OUTC
- Q26 pad 21: /LargeMotor/LargeBridgeC/PL -> /LargeMotor/LargeBridgeA/PL
- Q26 pad 22: /LargeMotor/LargeBridgeC/OUT -> /LargeMotor/OUTC
- Q26 pad 23: /LargeMotor/LargeBridgeC/PL -> /LargeMotor/LargeBridgeA/PL
- Q26 pad 24: /LargeMotor/LargeBridgeC/OUT -> /LargeMotor/OUTC
- Q26 pad 3: /LargeMotor/LargeBridgeC/PL -> /LargeMotor/LargeBridgeA/PL
- Q26 pad 4: /LargeMotor/LargeBridgeC/PL -> /LargeMotor/LargeBridgeA/PL
- Q26 pad 5: /LargeMotor/LargeBridgeC/PL -> /LargeMotor/LargeBridgeA/PL
- Q26 pad 6: /LargeMotor/LargeBridgeC/PL -> /LargeMotor/LargeBridgeA/PL
- Q26 pad 7: /LargeMotor/LargeBridgeC/PL -> /LargeMotor/LargeBridgeA/PL
- Q26 pad 8: /LargeMotor/LargeBridgeC/OUT -> /LargeMotor/OUTC
- Q26 pad 9: /LargeMotor/LargeBridgeC/PL -> /LargeMotor/LargeBridgeA/PL
- R15 pad 1: Net-(U7-IDRV) -> /LargeMotor/OUTA
- R15 pad 2: GND -> /WCPB
- R16 pad 1: Net-(U7-VDS) -> /WCPB
- R17 pad 1: Net-(U7-GAIN) -> Net-(U7-VDS)
- R17 pad 2: GND -> /SmallMotor1/DVDD
- R18 pad 1: Net-(U13-VOUT) -> /WSO
- R18 pad 2: /WSO -> Net-(U13-VOUT)
- R22 pad 1: Net-(U8-IDRV) -> /LargeMotor/OUTB
- R22 pad 2: GND -> /WCPB
- R23 pad 1: Net-(U8-VDS) -> /WCPB
- R24 pad 1: Net-(U8-GAIN) -> Net-(U8-VDS)
- R24 pad 2: GND -> /SmallMotor2/DVDD
- R25 pad 1: GND -> /WSO
- R25 pad 2: /WSO -> GND
- R29 pad 1: Net-(U9-IDRV) -> /LargeMotor/OUTC
- R29 pad 2: GND -> /WCPC
- R30 pad 1: Net-(U9-VDS) -> /WCPC
- R31 pad 1: Net-(U9-GAIN) -> Net-(U9-VDS)
- R31 pad 2: GND -> /SmallMotor3/DVDD
- R49 pad 1: /SmallMotor1/GLB -> /SmallMotor3/OUTA
- R49 pad 2: Net-(Q6-G) -> /CPA3
- R50 pad 1: /SmallMotor2/GLB -> /CPA3
- R50 pad 2: Net-(Q12-G) -> GND
- R51 pad 1: /SmallMotor3/GLB -> /SmallMotor1/OUTB
- R51 pad 2: Net-(Q18-G) -> /CPB1
- R52 pad 1: /SmallMotor1/GHB -> /CPB1
- R52 pad 2: Net-(Q5-G) -> GND
- R53 pad 1: /SmallMotor2/GHB -> /SmallMotor2/OUTB
- R53 pad 2: Net-(Q11-G) -> /CPB2
- R54 pad 1: /SmallMotor3/GHB -> /CPB2
- R54 pad 2: Net-(Q17-G) -> GND
- R55 pad 1: /SmallMotor1/GLC -> /SmallMotor3/OUTB
- R55 pad 2: Net-(Q8-G) -> /CPB3
- R56 pad 1: /SmallMotor2/GLC -> /CPB3
- R56 pad 2: Net-(Q14-G) -> GND
- R57 pad 1: /SmallMotor3/GLC -> /SmallMotor1/OUTC
- R57 pad 2: Net-(Q20-G) -> /CPC1
- R58 pad 1: /SmallMotor1/GHC -> /CPC1
- R58 pad 2: Net-(Q7-G) -> GND
- R59 pad 1: /SmallMotor2/GHC -> /SmallMotor2/OUTC
- R59 pad 2: Net-(Q13-G) -> /CPC2
- R60 pad 1: /SmallMotor3/GHC -> /CPC2
- R60 pad 2: Net-(Q19-G) -> GND
- U10 pad C1: /LargeMotor/LargeBridgeA/OUT -> /LargeMotor/OUTA
- U10 pad D4: /LargeMotor/LargeBridgeA/OUT -> /LargeMotor/OUTA
- U11 pad C1: /LargeMotor/LargeBridgeB/OUT -> /LargeMotor/OUTB
- U11 pad D4: /LargeMotor/LargeBridgeB/OUT -> /LargeMotor/OUTB
- U12 pad C1: /LargeMotor/LargeBridgeC/OUT -> /LargeMotor/OUTC
- U12 pad D4: /LargeMotor/LargeBridgeC/OUT -> /LargeMotor/OUTC
- U13 pad 5: unconnected-(U13-IP+-Pad5) -> /LargeMotor/LargeBridgeA/PL
- U13 pad 6: unconnected-(U13-IP--Pad6) -> GND
- U7 pad 14: /SmallMotor1/SHB -> /SmallMotor1/OUTB
- U7 pad 17: /SmallMotor1/SHC -> /SmallMotor1/OUTC
- U7 pad 27: Net-(U7-IDRV) -> unconnected-(U7-IDRV-Pad27)
- U7 pad 29: Net-(U7-GAIN) -> /SmallMotor1/DVDD
- U7 pad 33: Net-(U7-DVDD) -> /SmallMotor1/DVDD
- U7 pad 7: /SmallMotor1/SHA -> /SmallMotor1/OUTA
- U8 pad 14: /SmallMotor2/SHB -> /SmallMotor2/OUTB
- U8 pad 17: /SmallMotor2/SHC -> /SmallMotor2/OUTC
- U8 pad 27: Net-(U8-IDRV) -> unconnected-(U8-IDRV-Pad27)
- U8 pad 29: Net-(U8-GAIN) -> /SmallMotor2/DVDD
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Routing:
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- added copper zone on In1.Cu, net GND
- added copper zone on In2.Cu, net VDD

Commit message: Save layout
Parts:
- removed ? (x3): , 
- removed the C68 at (99.2, 54.9)
- removed the C68 at (99.1, 44.1)
- removed the C68 at (101.9, 49.2)
- removed the C68 at (101.9, 59.7)
- removed the C68 at (99.3, 33.6)
- removed C69, C70: 100n, Capacitor_SMD:C_0402_1005Metric
- removed C71: 22u, Capacitor_SMD:C_0805_2012Metric
- removed C72: 22u, Capacitor_SMD:C_0603_1608Metric
- removed REF** (x6): MountingHole_2.2mm_M2_DIN965_Pad, MountingHole:MountingHole_2.2mm_M2_DIN965_Pad
- added C62: 2m2, User_Footprints:C_D10xL16_Horizontal, B.Cu at (100.7, 40.5)
- added C63: 100n, Capacitor_SMD:C_0402_1005Metric, F.Cu at (113.7, 58.8)
- added C65: 2m2, User_Footprints:C_D10xL16_Horizontal, B.Cu at (99.2, 53.0)
- added C66: 2m2, User_Footprints:C_D10xL16_Horizontal, B.Cu at (100.7, 50.5)
- added J10: Conn_01x01_Pin, User_Footprints:Pad-P1.5, F.Cu at (120.6, 38.1)
- added J11: Conn_01x01_Pin, User_Footprints:Pad-P1.5, F.Cu at (66.4, 45.4)
- added J12: Conn_01x01_Pin, MountingHole:MountingHole_3.2mm_M3_Pad_Via, F.Cu at (103.6, 31.0)
- added J3: Conn_01x01_Pin, User_Footprints:Pad-P1.5, F.Cu at (80.5, 37.3)
- added J4: Conn_01x01_Pin, User_Footprints:Pad-P1.5, F.Cu at (115.0, 34.9)
- added J5: Conn_01x01_Pin, User_Footprints:Pad-P1.5, F.Cu at (60.8, 48.6)
- added J6: Conn_01x01_Pin, User_Footprints:Pad-P1.5, F.Cu at (74.8, 40.6)
- added J7: Conn_01x01_Pin, User_Footprints:Pad-P1.5, F.Cu at (109.4, 31.8)
- added J8: Conn_01x01_Pin, User_Footprints:Pad-P1.5, F.Cu at (55.2, 51.8)
- added J9: Conn_01x01_Pin, User_Footprints:Pad-P1.5, F.Cu at (86.2, 34.3)
- AE1: value Antenna -> Antenna_Chip
- C18: moved to B.Cu
- C68: footprint Capacitor_THT:C_Radial_D10.0mm_H16.0mm_P5.00mm -> User_Footprints:C_D10xL16_Horizontal
- J1: value Conn_01x02_Pin -> Conn_01x01_Pin; footprint Connector_AMASS:AMASS_XT30PW-M_1x02_P2.50mm_Horizontal -> MountingHole:MountingHole_3.2mm_M3_Pad_Via
- moved R41 89.0 mm to (67.1, 60.7)
- moved R42 89.0 mm to (67.1, 62.7)
- moved Q2 88.2 mm to (64.4, 61.7), turned to 90 degrees
- moved C67 80.6 mm to (65.0, 59.3)
- moved C76 78.2 mm to (109.0, 61.3), turned to -90 degrees
- moved R30 72.3 mm to (81.8, 58.4)
- moved L1 71.5 mm to (107.4, 45.6), turned to 180 degrees
- moved R29 70.4 mm to (82.1, 61.6), turned to 0 degrees
- moved R1 69.8 mm to (118.6, 48.3), turned to 90 degrees
- moved C80 69.3 mm to (82.4, 60.0)
- moved R2 67.6 mm to (117.6, 48.3), turned to -90 degrees
- moved C77 67.3 mm to (89.0, 56.4)
- moved R15 65.2 mm to (93.4, 60.9), turned to 180 degrees
- moved U15 65.2 mm to (112.7, 61.1)
- moved R18 64.9 mm to (87.0, 54.9)
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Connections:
- AE1 pad 2: (no net) -> unconnected-(AE1-PCB_Trace-Pad2)
- C68 pad 1: VDD -> GND
- C68 pad 2: GND -> VDD
- J1 pad 1: VDD -> GND
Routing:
- net /LargeMotor/OUTC: vias 0 -> 28
- net /LargeMotor/OUTB: vias 0 -> 28
- net /LargeMotor/OUTA: vias 0 -> 28
- added copper zone on B.Cu, net /LargeMotor/OUTA
- added copper zone on B.Cu, net /LargeMotor/OUTB
- added copper zone on B.Cu, net /LargeMotor/OUTC
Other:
- board size 99.2 x 51.2 mm -> 93.9 x 48.4 mm
- board text added: "Please Don't Explode 9000"
